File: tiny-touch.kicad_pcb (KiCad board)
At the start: 2 copper layers, 118 parts, among them IC1 STM32F072VBT6, Q1 DTC123J, SW1 SW_Push, U1 MCP1700-3002E_SOT23, U2 SRV05-4

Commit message: Simplify layout
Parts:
- moved U1 173.9 mm to (125.8, 63.7), turned to 90 degrees
- moved R1 150.9 mm to (163.9, 70.2)
- moved R2 143.4 mm to (159.6, 70.2)
- moved R5 137.5 mm to (159.5, 74.7)
- moved U2 136.7 mm to (172.1, 61.7)
- moved R4 133.5 mm to (163.9, 74.7)
- moved D2 132.1 mm to (121.3, 66.0), turned to 90 degrees
- moved C11 131.8 mm to (171.4, 72.7)
- moved C9 129.1 mm to (179.7, 72.7)
- moved C3 128.3 mm to (183.7, 68.5)
- moved R3 127.2 mm to (155.4, 70.2)
- moved R6 126.5 mm to (155.5, 74.7)
- moved C1 117.1 mm to (192.1, 68.5)
- moved C7 117.0 mm to (187.8, 72.6)
- moved D1 113.0 mm to (121.3, 61.0), turned to 180 degrees
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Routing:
- added copper zone on B.Cu, net GND
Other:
- board outline added: 99.8 x 83.2 mm

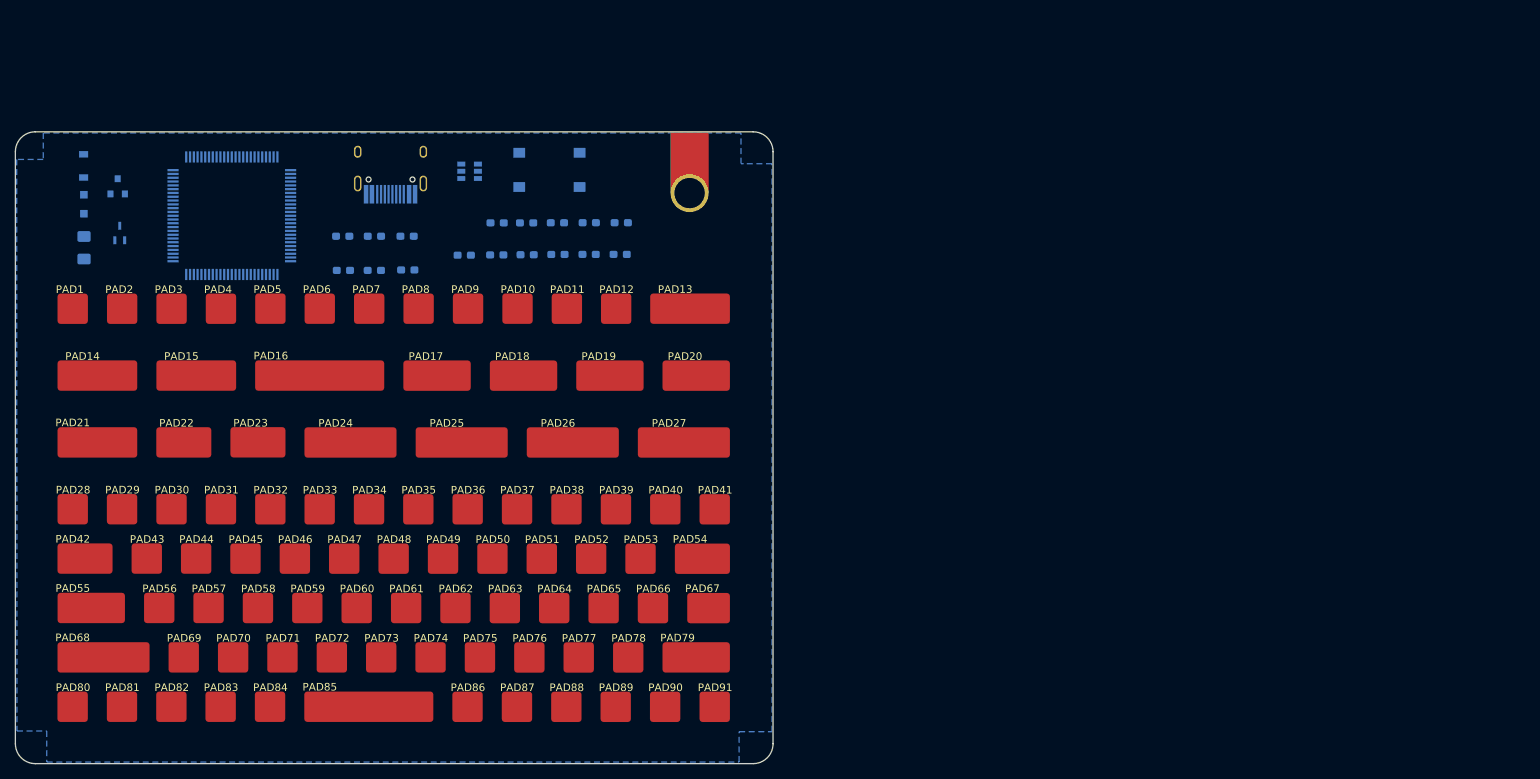
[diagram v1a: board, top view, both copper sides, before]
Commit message: Route major power lines
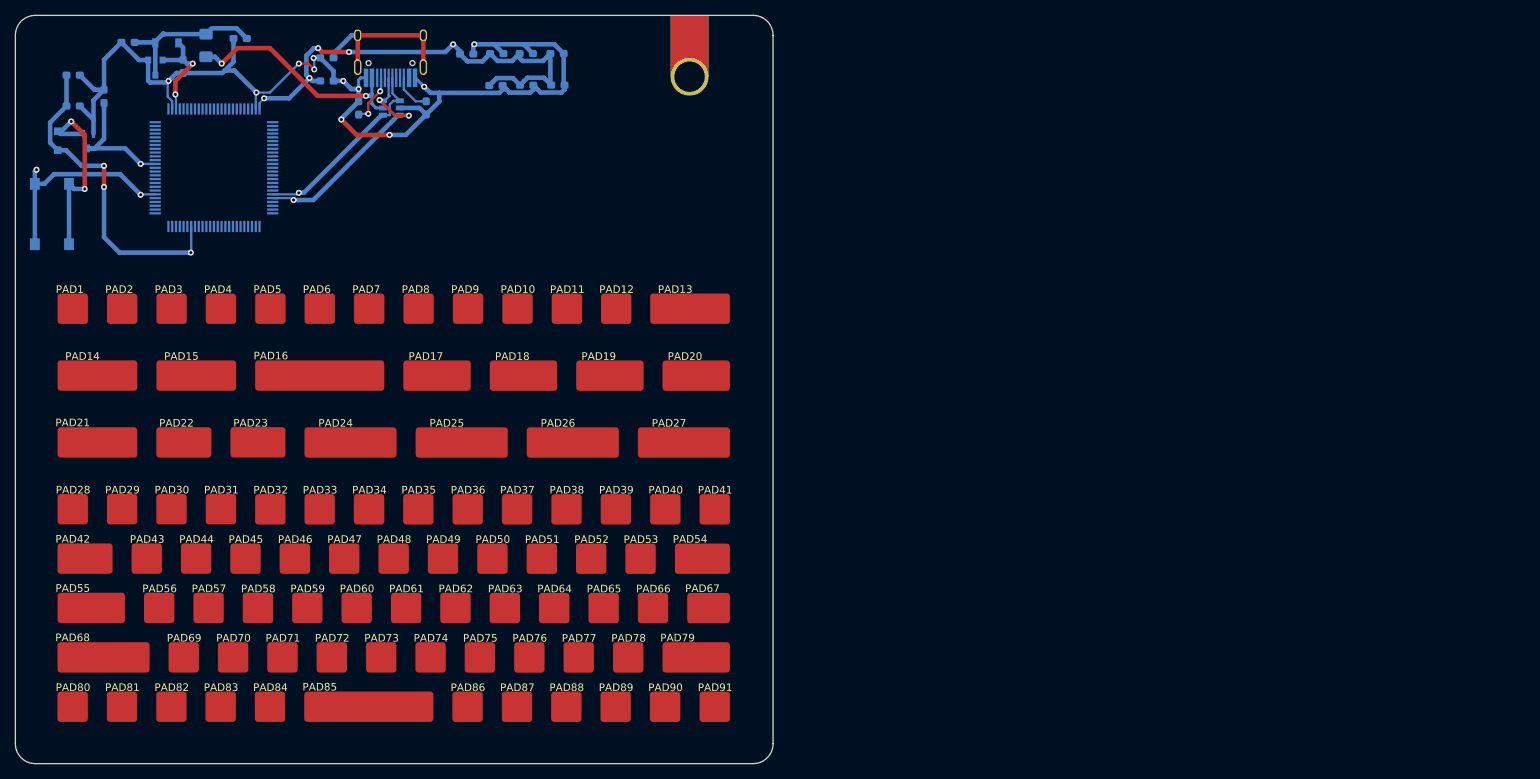
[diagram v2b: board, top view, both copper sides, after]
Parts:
- moved SW1 65.8 mm to (117.1, 67.3), turned to 270 degrees
- moved C2 65.2 mm to (127.1, 44.7), turned to 180 degrees
- moved C1 61.3 mm to (134.4, 47.9), turned to 90 degrees
- moved C10 60.6 mm to (119.9, 49.0)
- moved C11 51.8 mm to (124.0, 51.8), turned to 90 degrees
- moved R4 49.1 mm to (119.9, 53.1)
- moved R1 34.1 mm to (141.9, 44.2)
- moved C6 33.2 mm to (171.7, 46.2)
- moved PF1 31.1 mm to (137.4, 45.1), turned to 270 degrees
- moved R6 24.0 mm to (166.4, 53.3), turned to 90 degrees
- moved R3 23.6 mm to (153.3, 46.7)
- moved C7 22.7 mm to (183.7, 50.3)
- moved C8 22.7 mm to (179.6, 50.3)
- moved C9 22.7 mm to (175.6, 50.4)
- moved C3 22.3 mm to (183.6, 46.2)
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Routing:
- net GND: track 0.00 -> 146.2 mm, vias 0 -> 11
- net +3V3: track 0.00 -> 105.1 mm, vias 0 -> 9
- net BOOTO: track 0.00 -> 43.3 mm, vias 0 -> 3
- net D+: track 0.00 -> 31.5 mm, vias 0 -> 3
- net VBUS: track 0.00 -> 30.9 mm, vias 0 -> 2
- net D-: track 0.00 -> 26.0 mm, vias 0 -> 1
- net Net-(D2-Pad2): track 0.00 -> 25.8 mm, vias 0 -> 2
- net GNDREF: track 0.00 -> 21.7 mm
- net +5V: track 0.00 -> 20.5 mm
- net NRST: track 0.00 -> 16.9 mm, vias 0 -> 1
- net Net-(R5-Pad2): track 0.00 -> 6.74 mm, vias 0 -> 2
- net Net-(R6-Pad2): track 0.00 -> 5.11 mm
- added copper zone on In1.Cu, net +3V3
- added copper zone on In2.Cu, net GND
- removed copper zone on B.Cu, net GND
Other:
- board size 99.8 x 83.2 mm -> 99.8 x 98.5 mm
- copper layers 2 -> 4

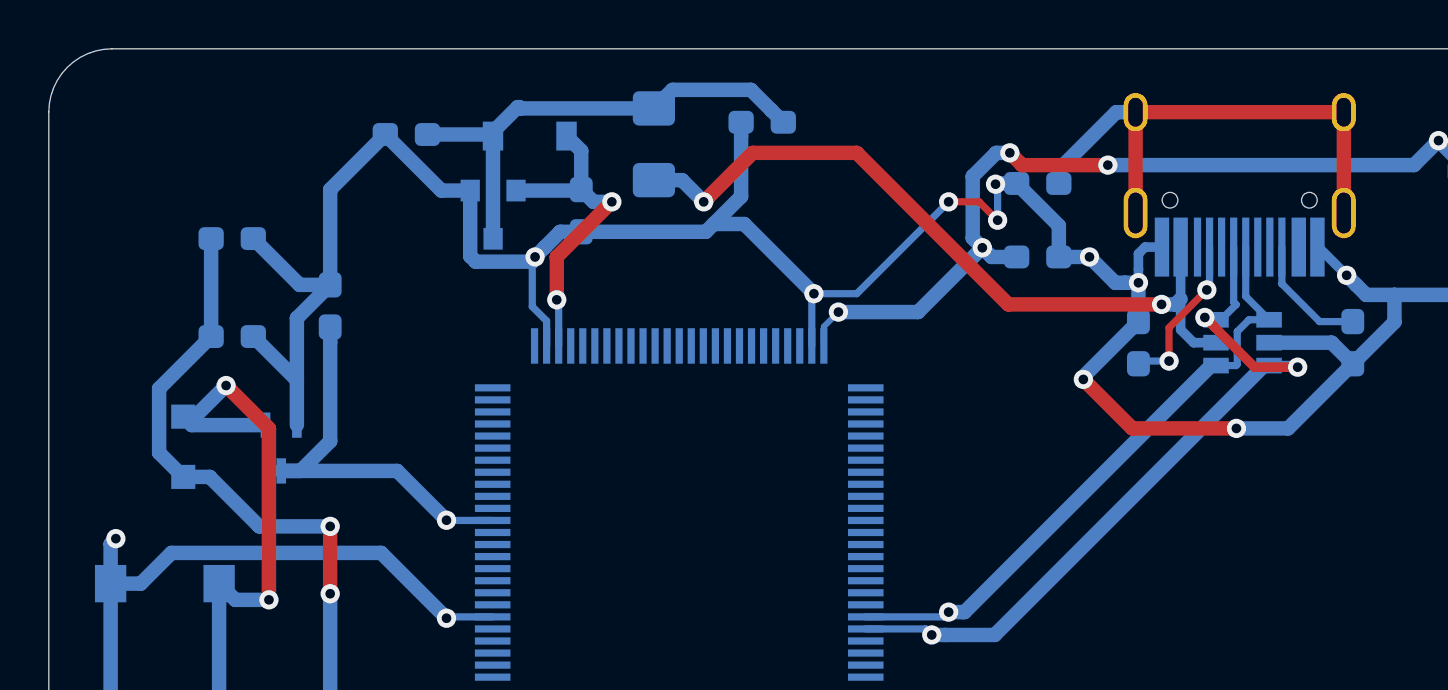
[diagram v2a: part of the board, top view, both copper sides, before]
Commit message: Back to 2 layer
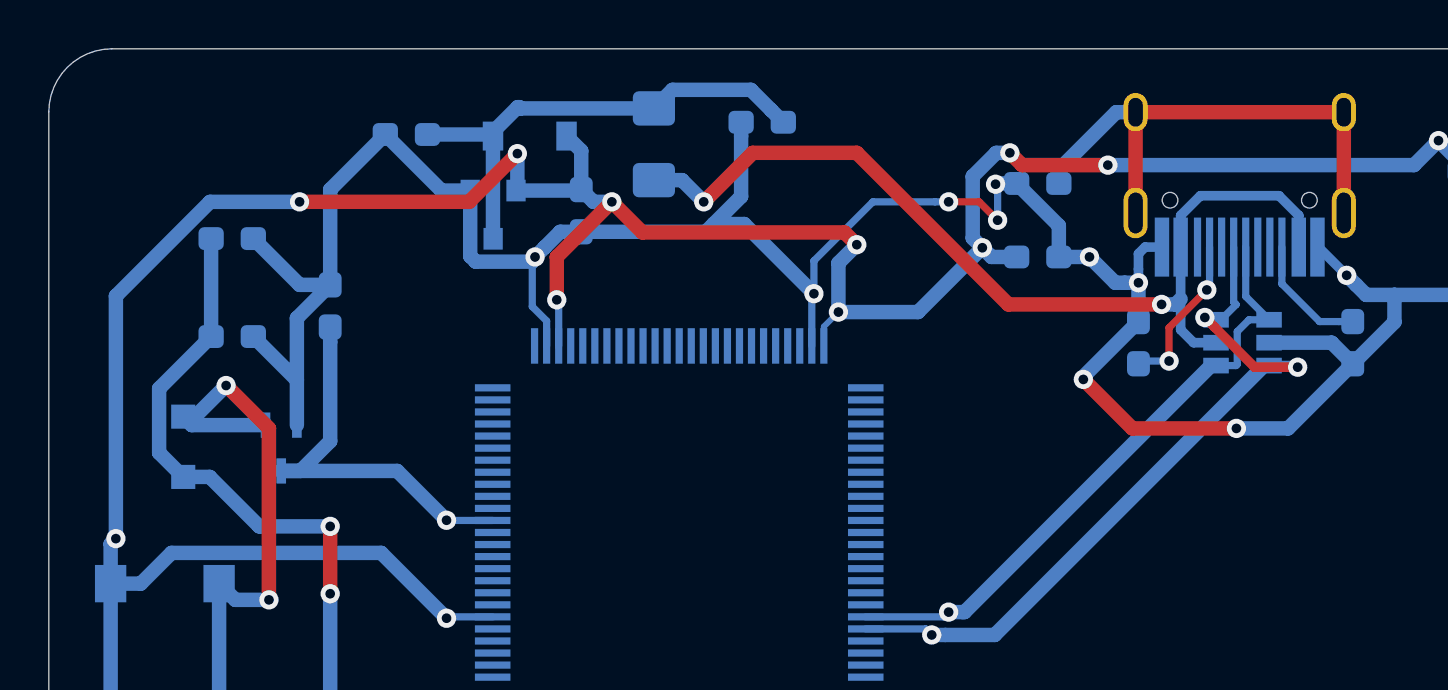
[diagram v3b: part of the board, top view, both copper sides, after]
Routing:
- net +3V3: track 105.1 -> 149.9 mm, vias 9 -> 12
- net VBUS: track 30.9 -> 39.1 mm
- net GND: track 146.2 -> 147.0 mm
- removed copper zone on In1.Cu, net +3V3
- removed copper zone on In2.Cu, net GND
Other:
- copper layers 4 -> 2
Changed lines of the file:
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@@
     (thickness 1.6)
     (drawings 8)
-    (tracks 282)
+    (tracks 304)
     (zones 0)
     (modules 118)
@@
   (layers
     (0 F.Cu signal)
-    (1 In1.Cu signal)
-    (2 In2.Cu signal)
     (31 B.Cu signal)
     (32 B.Adhes user)
@@
   )
   (setup
-    (last_trace_width 0.3)
+    (last_trace_width 0.4)
     (user_trace_width 0.2)
     (user_trace_width 0.3)
@@
   (segment (start 134.874 47.498) (end 134.366 46.99) (width 0.6) (layer B.Cu) (net 1))
   (segment (start 135.636 47.498) (end 134.874 47.498) (width 0.6) (layer B.Cu) (net 1))
+  (via (at 145.796 49.276) (size 0.8) (drill 0.4) (layers F.Cu B.Cu) (net 1))
+  (segment (start 145.034 50.038) (end 145.796 49.276) (width 0.6) (layer B.Cu) (net 1))
+  (segment (start 145.034 52.07) (end 145.034 50.038) (width 0.6) (layer B.Cu) (net 1))
+  (segment (start 145.796 49.276) (end 145.288 48.768) (width 0.6) (layer F.Cu) (net 1))
+  (segment (start 136.906 48.768) (end 135.636 47.498) (width 0.6) (layer F.Cu) (net 1))
+  (segment (start 145.288 48.768) (end 136.906 48.768) (width 0.6) (layer F.Cu) (net 1))
+  (segment (start 115.062 51.405002) (end 118.969002 47.498) (width 0.6) (layer B.Cu) (net 1))
+  (segment (start 115.062 61.468) (end 115.062 51.405002) (width 0.6) (layer B.Cu) (net 1))
+  (via (at 122.682 47.498) (size 0.8) (drill 0.4) (layers F.Cu B.Cu) (net 1))
+  (segment (start 118.969002 47.498) (end 122.682 47.498) (width 0.6) (layer B.Cu) (net 1))
+  (segment (start 129.715679 47.498) (end 131.716331 45.497348) (width 0.6) (layer F.Cu) (net 1))
+  (via (at 131.716331 45.497348) (size 0.8) (drill 0.4) (layers F.Cu B.Cu) (net 1))
+  (segment (start 122.682 47.498) (end 129.715679 47.498) (width 0.6) (layer F.Cu) (net 1))
+  (segment (start 131.716331 46.973669) (end 131.66 47.03) (width 0.6) (layer B.Cu) (net 1))
+  (segment (start 131.716331 45.497348) (end 131.716331 46.973669) (width 0.6) (layer B.Cu) (net 1))
   (via (at 155.448 49.784) (size 0.8) (drill 0.4) (layers F.Cu B.Cu) (net 2))
   (segment (start 154.178 49.784) (end 155.448 49.784) (width 0.6) (layer B.Cu) (net 2))
@@
   (segment (start 143.93 53.476) (end 143.93 51.396) (width 0.3) (layer B.Cu) (net 2))
   (via (at 149.606 47.498) (size 0.8) (drill 0.4) (layers F.Cu B.Cu) (net 2))
-  (segment (start 145.796 51.308) (end 149.606 47.498) (width 0.3) (layer B.Cu) (net 2))
-  (segment (start 144.018 51.308) (end 145.796 51.308) (width 0.3) (layer B.Cu) (net 2))
   (segment (start 150.876 47.498) (end 151.638 48.26) (width 0.3) (layer F.Cu) (net 2))
   (via (at 151.638 48.26) (size 0.8) (drill 0.4) (layers F.Cu B.Cu) (net 2))
@@
   (segment (start 134.366 48.74) (end 133.49399 48.74) (width 0.6) (layer B.Cu) (net 2))
   (segment (start 132.334314 49.980001) (end 132.44999 49.864325) (width 0.6) (layer B.Cu) (net 2))
+  (segment (start 144.018 51.308) (end 144.018 49.943996) (width 0.3) (layer B.Cu) (net 2))
+  (segment (start 149.040315 47.498) (end 149.606 47.498) (width 0.3) (layer B.Cu) (net 2))
+  (segment (start 144.018 49.943996) (end 146.463996 47.498) (width 0.3) (layer B.Cu) (net 2))
+  (segment (start 146.463996 47.498) (end 149.040315 47.498) (width 0.3) (layer B.Cu) (net 2))
   (segment (start 142.248928 43.696928) (end 142.748 44.196) (width 0.6) (layer B.Cu) (net 3))
   (segment (start 141.403153 42.851153) (end 142.248928 43.696928) (width 0.6) (layer B.Cu) (net 3))
@@
   (segment (start 159.23 51.534) (end 159.23 52.802) (width 0.4) (layer B.Cu) (net 95))
   (segment (start 159.23 49.375) (end 159.23 51.534) (width 0.4) (layer B.Cu) (net 95))
+  (segment (start 159.23 48.063002) (end 160.049002 47.244) (width 0.4) (layer B.Cu) (net 95))
+  (segment (start 159.23 49.375) (end 159.23 48.063002) (width 0.4) (layer B.Cu) (net 95))
+  (segment (start 164.13 48.063002) (end 164.13 49.375) (width 0.4) (layer B.Cu) (net 95))
+  (segment (start 163.310998 47.244) (end 164.13 48.063002) (width 0.4) (layer B.Cu) (net 95))
+  (segment (start 160.049002 47.244) (end 163.310998 47.244) (width 0.4) (layer B.Cu) (net 95))
   (segment (start 166 47.96) (end 166 43.78) (width 0.6) (layer F.Cu) (net 96))
   (segment (start 157.36 47.96) (end 157.36 43.78) (width 0.6) (layer F.Cu) (net 96))
@@
   (segment (start 163.43 50.9) (end 164.995 52.465) (width 0.3) (layer B.Cu) (net 98))
   (segment (start 163.43 49.375) (end 163.43 50.9) (width 0.3) (layer B.Cu) (net 98))
-  (zone (net 2) (net_name GND) (layer In2.Cu) (hatch edge 0.508)
-    (connect_pads (clearance 0.508))
-    (min_thickness 0.254)
-    (fill yes (arc_segments 32) (thermal_gap 0.508) (thermal_bridge_width 0.508))
-    (polygon
-      (pts
-        (xy 112.268 41.148) (xy 112.268 139.7) (xy 212.09 139.7) (xy 212.09 41.148)
-      )
-    )
-  )
-  (zone (net 1) (net_name +3V3) (layer In1.Cu) (hatch edge 0.508)
-    (connect_pads (clearance 0.508))
-    (min_thickness 0.254)
-    (fill yes (arc_segments 32) (thermal_gap 0.508) (thermal_bridge_width 0.508))
-    (polygon
-      (pts
-        (xy 112.268 41.148) (xy 112.268 139.7) (xy 212.09 139.7) (xy 212.09 41.148)
-      )
-    )
-  )
 )

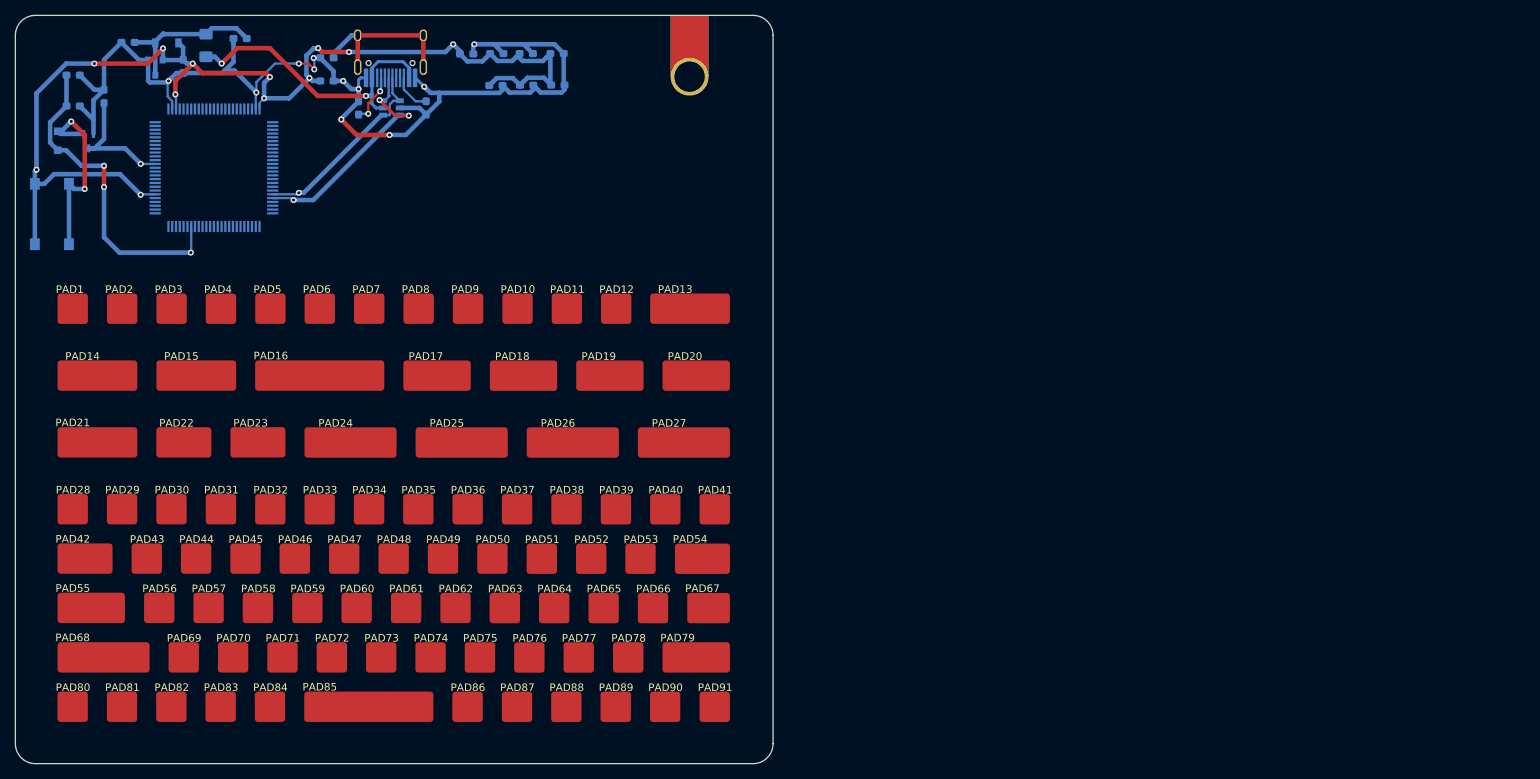
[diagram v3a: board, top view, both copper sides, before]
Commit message: 2-layer auto-routed with FreeRouting
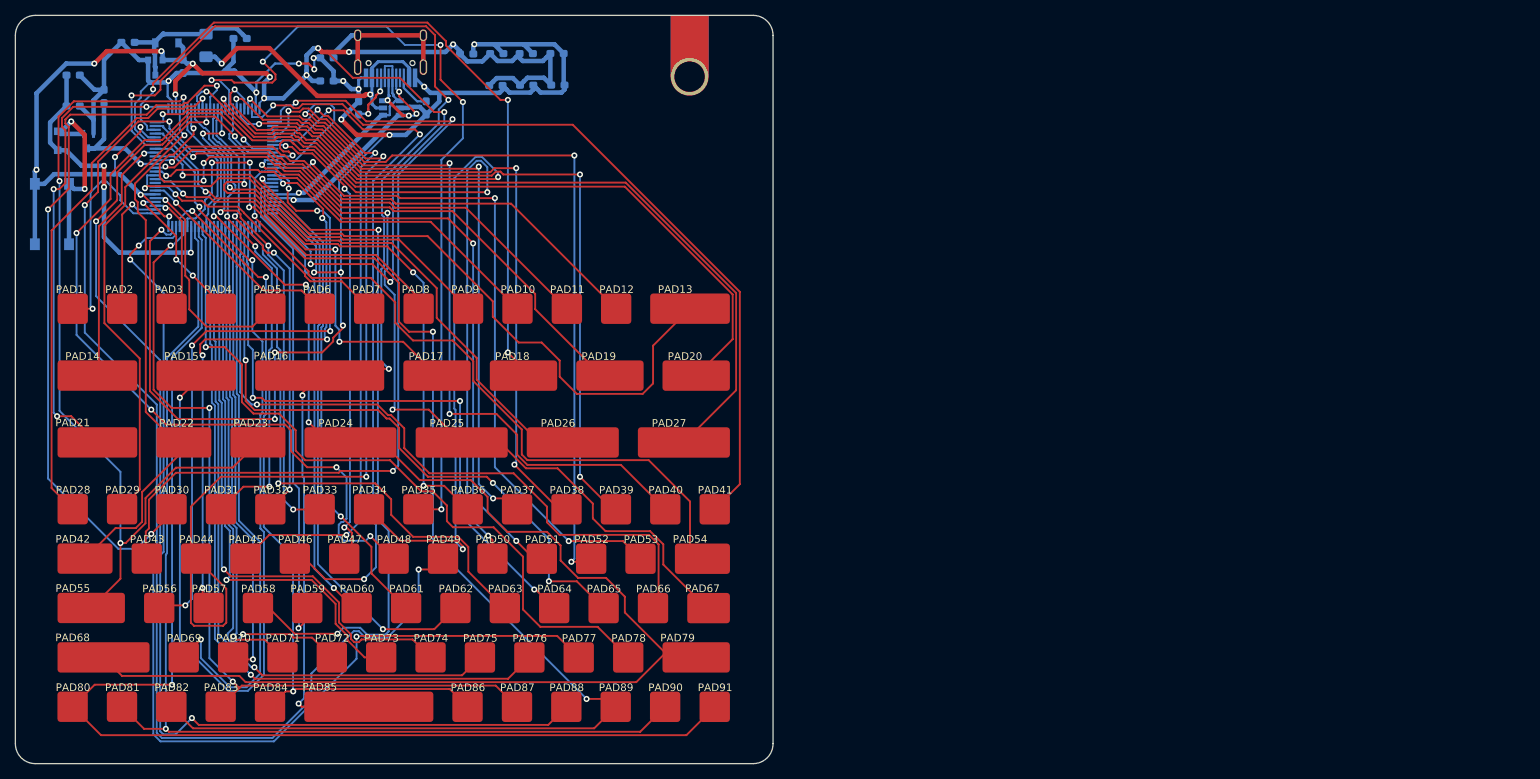
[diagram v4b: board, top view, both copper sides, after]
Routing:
- net A6: track 0.00 -> 195.2 mm, vias 0 -> 3
- net B8: track 0.00 -> 177.1 mm, vias 0 -> 5
- net B4: track 0.00 -> 175.2 mm, vias 0 -> 3
- net F2: track 0.00 -> 165.8 mm, vias 0 -> 5
- net B6: track 0.00 -> 164.1 mm, vias 0 -> 1
- net D12: track 0.00 -> 157.7 mm, vias 0 -> 3
- net B7: track 0.00 -> 142.3 mm, vias 0 -> 1
- net A7: track 0.00 -> 129.1 mm, vias 0 -> 5
- net E1: track 0.00 -> 128.9 mm, vias 0 -> 3
- net C3: track 0.00 -> 127.5 mm, vias 0 -> 3
- net B15: track 0.00 -> 118.2 mm, vias 0 -> 3
- net B12: track 0.00 -> 118.2 mm, vias 0 -> 3
- net GND: track 147.0 -> 262.8 mm, vias 11 -> 17
- net E10: track 0.00 -> 115.1 mm, vias 0 -> 3
- net A5: track 0.00 -> 114.2 mm, vias 0 -> 3
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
